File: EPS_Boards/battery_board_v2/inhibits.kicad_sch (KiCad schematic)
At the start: 39 parts, among them J4 Conn_01x08_Male, J5 RBF, J6 RBF Deployment Bypass, J7 30s Timer, U3 TPS63000-Q1, U4 LTC6995HS6-1#TRMPBF, U5 LTC6995HS6-1#TRMPBF, U6 74AUP1G08, U7 UCC2946D

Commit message: eps: battery board: progress on pcb layout
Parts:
- U7: footprint SOIC127P599X175-8N -> qset-footprints:SOIC127P600X175-8N
- gave numbers to parts that had none: 1
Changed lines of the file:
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@@
     (property "Reference" "U7" (id 0) (at 220.345 21.59 0))
     (property "Value" "UCC2946D" (id 1) (at 220.345 24.13 0))
-    (property "Footprint" "SOIC127P599X175-8N" (id 2) (at 220.345 40.005 0)
+    (property "Footprint" "qset-footprints:SOIC127P600X175-8N" (id 2) (at 220.345 40.005 0)
       (effects (font (size 1.27 1.27)) (justify bottom) hide)
     )
@@
   (symbol (lib_id "power:GND") (at 37.719 41.783 0) (unit 1)
     (in_bom yes) (on_board yes) (fields_autoplaced)
-    (property "Reference" "#PWR?" (id 0) (at 37.719 48.133 0)
+    (property "Reference" "#PWR0120" (id 0) (at 37.719 48.133 0)
       (effects (font (size 1.27 1.27)) hide)
     )
@@
   (symbol (lib_id "Device:D_TVS") (at 37.719 34.671 90) (mirror x) (unit 1)
     (in_bom yes) (on_board yes)
-    (property "Reference" "D?" (id 0) (at 32.639 32.766 90)
+    (property "Reference" "D3" (id 0) (at 32.639 32.766 90)
       (effects (font (size 1.27 1.27)) (justify right))
     )

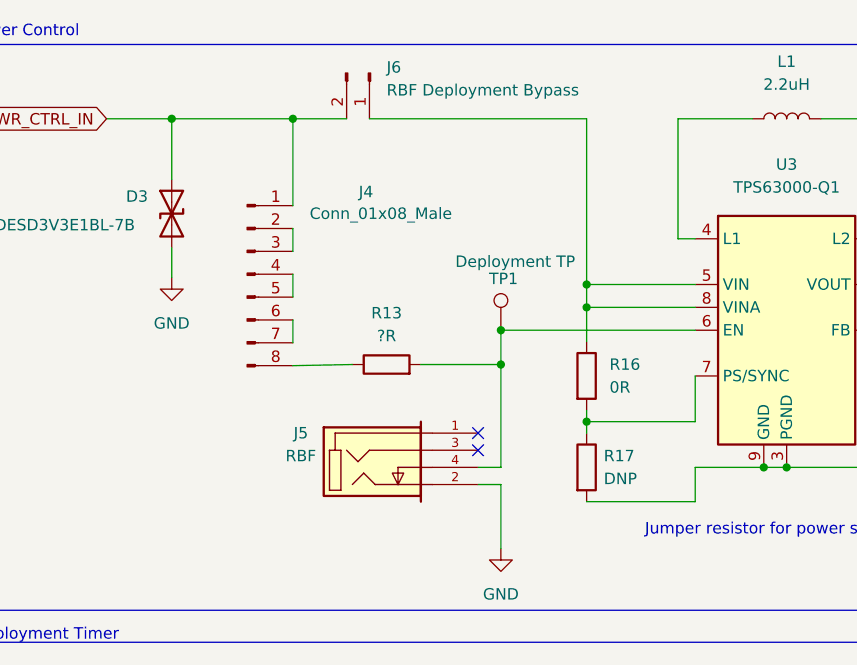
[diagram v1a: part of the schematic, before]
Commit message: eps: battery board: RBF bypass changes
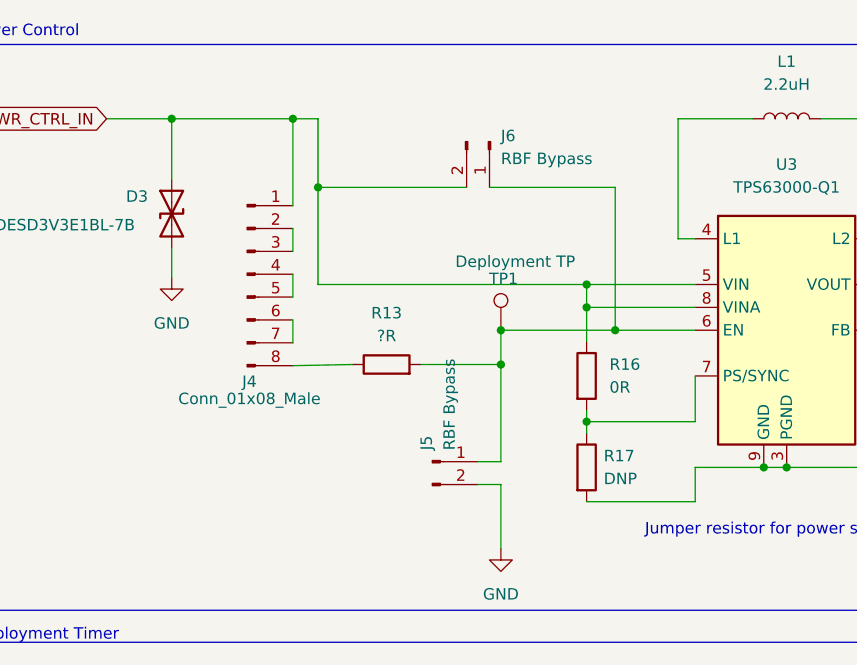
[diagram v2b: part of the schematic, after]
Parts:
- removed J5: RBF, qset-footprints:CUI_SJ1-3524NG, symbol SJ1-3524NG:SJ1-3524NG
- added J5: RBF Bypass, Connector_PinHeader_2.00mm:PinHeader_1x02_P2.00mm_Horizontal, symbol Connector:Conn_01x02_Male
- J6: value RBF Deployment Bypass -> RBF Bypass
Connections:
- net GND: now also J5.2 (Pin_2)
- net PWR_CTRL_IN: now also R16.1, U3.5 (VIN), U3.8 (VINA)
- net at R13.2, TP1.1, U3.6 (EN): now also J6.1 (Pin_1), J5.1 (Pin_1)
- no-connect marks 3 -> 1
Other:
- moved on the sheet: J6

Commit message: eps: battery board: second design review changes
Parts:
- removed D3: DESD3V3E1BL-7B, Resistor_SMD:R_0201_0603Metric, symbol Device:D_TVS
- removed J7: 30s Timer, Connector_PinHeader_2.00mm:PinHeader_1x02_P2.00mm_Horizontal, symbol Connector:Conn_01x02_Male
- removed R13: ?R, Resistor_SMD:R_0402_1005Metric, symbol Device:R
- removed R16: 0R, Resistor_SMD:R_0402_1005Metric, symbol Device:R
- removed R17: DNP, Resistor_SMD:R_0402_1005Metric, symbol Device:R
- removed R18, R19: 100k, Resistor_SMD:R_0402_1005Metric, symbol Device:R
- removed U3: TPS63000-Q1, Package_SON:Texas_DRC0010J_ThermalVias, symbol Regulator_Switching:TPS63000-Q1
- added C?: 0.1 uF, Capacitor_SMD:C_01005_0402Metric, symbol Device:C
- added C? (x2): 22 uF, Capacitor_SMD:C_01005_0402Metric, symbol Device:C
- added J?: Deployment Timer, symbol Connector:Conn_01x03_Male
- added J?: Watchdog Timer, symbol Connector:Conn_01x03_Male
- added R? (x2): 1 M, symbol Device:R
- added R?: 920k, Resistor_SMD:R_0402_1005Metric, symbol Device:R
- added U3: TPS63060, Package_SON:Texas_S-PWSON-N10_ThermalVias, symbol Regulator_Switching:TPS63060
- C12: value C -> 22 uF
- J5: value RBF Bypass -> RBF
- J6: value RBF Bypass -> Deployment Switch Bypass
- R10: value 412k -> 920k
- R12: value 390k -> 681k
- R15: value 887k -> 681k
- R22: value 100k -> 681k
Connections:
- net GND: now also U4.1 (RST/~{RST}), C?.2, C?.2, C?.2, R?.2, R?.2, U3.11 (PGND), U3.4 (PS/SYNC), U3.5 (PG), U3.7 (GND)
- net PWR_CTRL_IN: now also U3.2 (VIN)
- net VCC: now also C?.1, C?.1, R?.1, U3.9 (VOUT)
- net nRST_HB: no longer U5.1 (RST/~{RST})
- net at J5.1 (Pin_1), TP1.1: now also R?.2, U3.3 (EN); no longer J6.1 (Pin_1)
- net at L1.1: now also U3.1 (L1)
- net at L1.2: now also U3.10 (L2)
- net at R10.1: now also J?.1 (Pin_1)
- net at R20.2, R21.1: now also U3.8 (FB)
- net at J4.8 (Pin_8): now also J6.1 (Pin_1), R?.1
- net at R11.2, R12.1, U5.4 (DIV): now also J?.2 (Pin_2)
- net at R14.2, R15.1, U4.4 (DIV): now also J?.2 (Pin_2)
- net HB renamed EPS_INT
- net EPS_INT: now also U5.1 (RST/~{RST})
- new net: C?.1, U3.6 (VAUX)
- new net: J?.1 (Pin_1), R?.1
- no-connect marks 1 -> 4
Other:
- note removed: "Confirm NC on nRES & VDD is 3V3_CON instead of GND"
- note removed: "Jumper resistor for power save mode."
- note removed: "Review SET resistor"
- moved on the sheet: C10, C11, C12, J4, J5, J6, L1, R10, R11, R12, R20, R21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

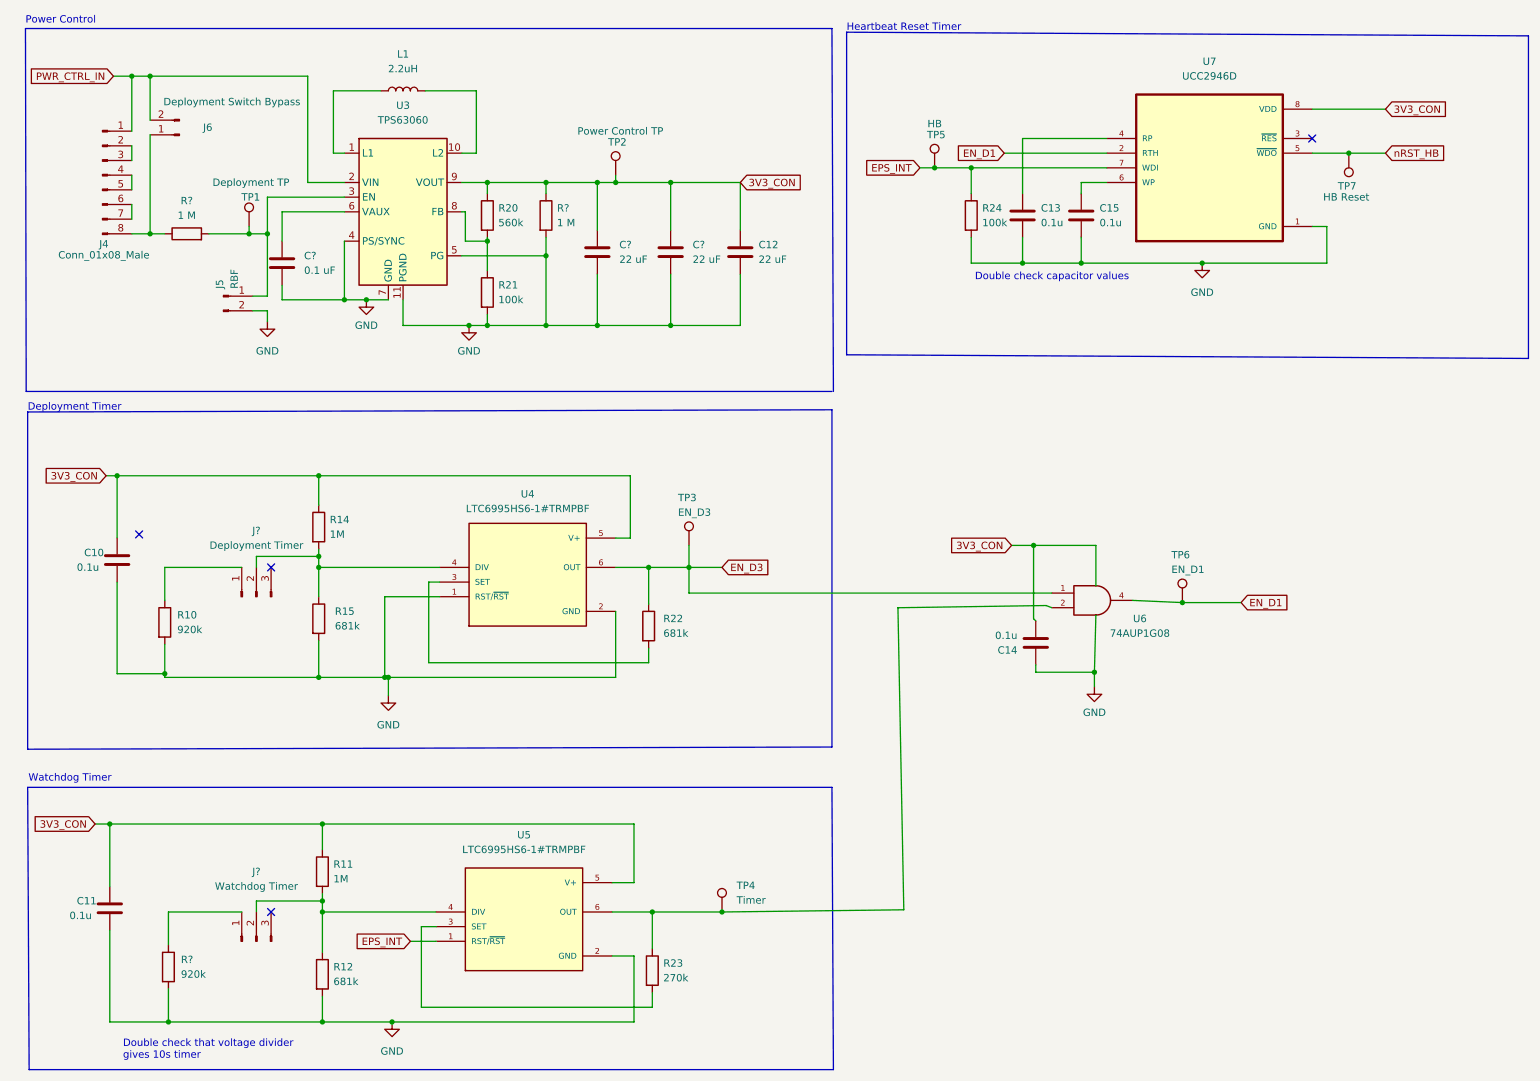
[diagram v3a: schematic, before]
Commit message: eps: battery board: more design review changes
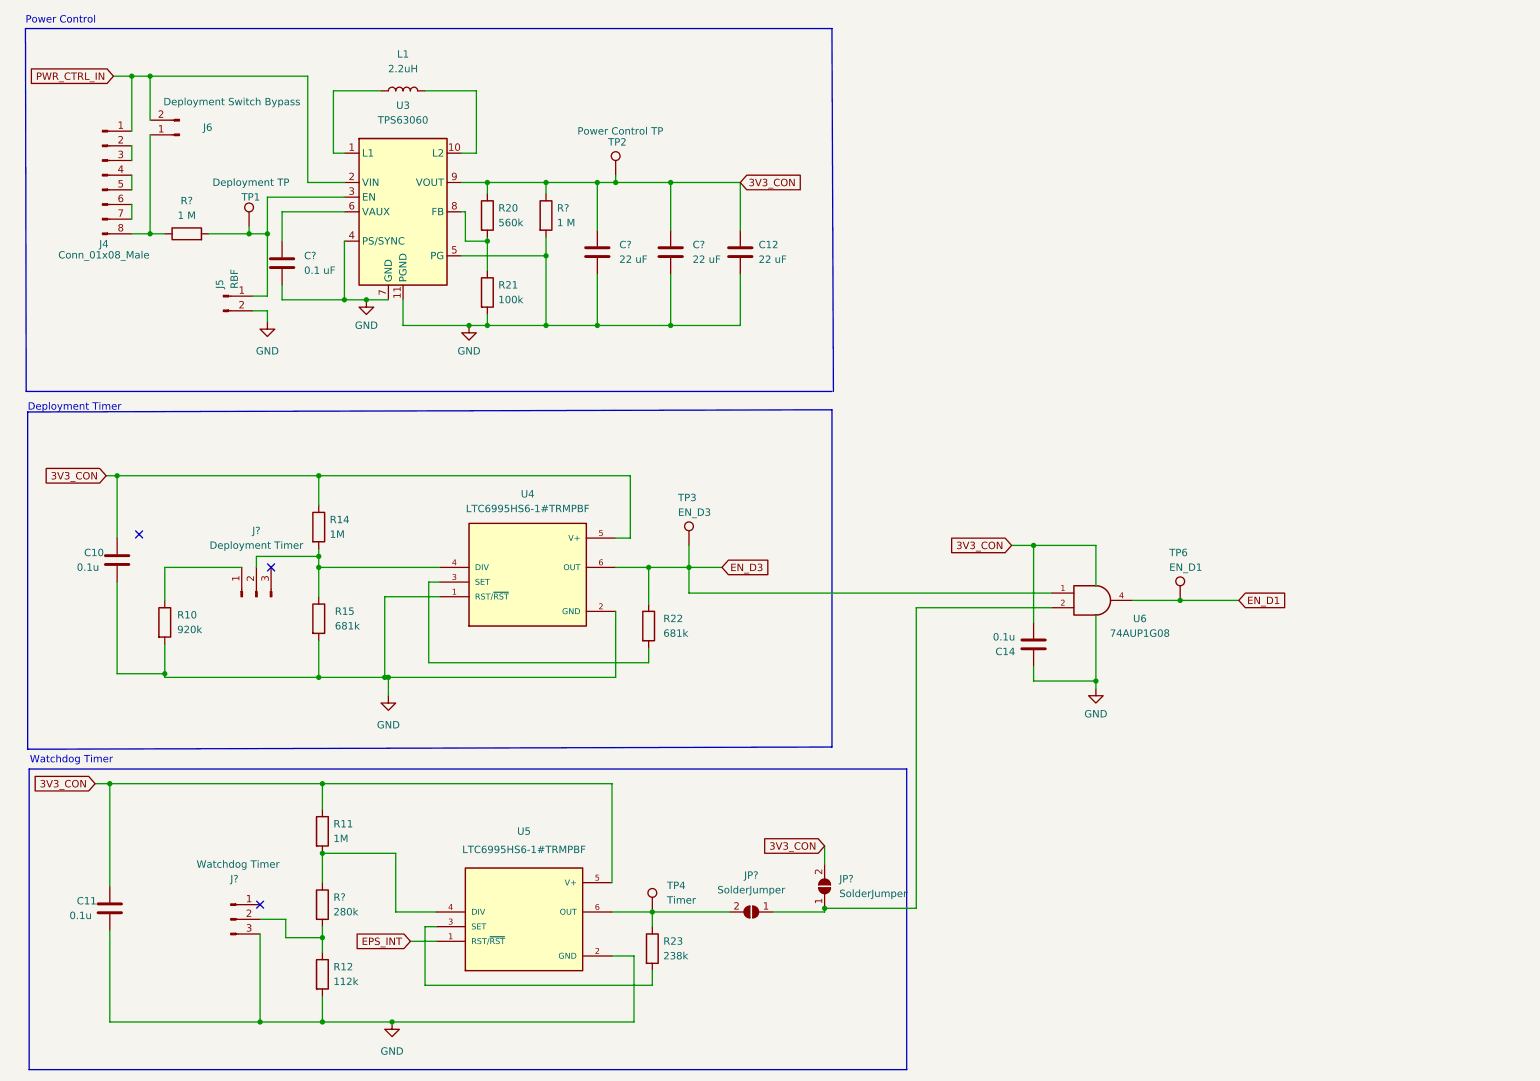
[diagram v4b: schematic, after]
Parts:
- removed C13, C15: 0.1u, Capacitor_SMD:C_01005_0402Metric, symbol Device:C
- removed R24: 100k, Resistor_SMD:R_0402_1005Metric, symbol Device:R
- removed TP5: HB, TestPoint:TestPoint_Pad_D2.0mm, symbol Connector:TestPoint
- removed TP7: HB Reset, TestPoint:TestPoint_Pad_D2.0mm, symbol Connector:TestPoint
- removed U7: UCC2946D, qset-footprints:SOIC127P600X175-8N, symbol UCC2946D:UCC2946D
- added JP? (x2): SolderJumper, Jumper:SolderJumper-2_P1.3mm_Open_Pad1.0x1.5mm, symbol Jumper:SolderJumper_2_Open
- R12: value 681k -> 112k
- R23: value 270k -> 238k
- R?: value 920k -> 280k
- U6: footprint qset-footprints:SOT65P210X110-5N -> Package_TO_SOT_SMD:SOT-353_SC-70-5_Handsoldering
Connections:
- net GND: now also J?.3 (Pin_3); no longer R?.2
- net VCC: now also JP?.2 (B)
- net at R11.2, U5.4 (DIV): now also R?.1; no longer J?.2 (Pin_2), R12.1
- net at R23.1, TP4.1, U5.6 (OUT): now also JP?.2 (B); no longer U6.2
- net at J?.1 (Pin_1): no longer R?.1
- new net: JP?.1 (A), JP?.1 (A), U6.2
- new net: J?.2 (Pin_2), R12.1, R?.2
- no-connect marks 4 -> 3
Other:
- note removed: "Double check capacitor values"
- note removed: "Double check that voltage divider gives 10s timer"
- note removed: "Heartbeat Reset Timer"
- moved on the sheet: J?, R11, R23, R?, TP4, TP6
